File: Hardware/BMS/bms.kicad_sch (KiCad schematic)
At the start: 25 parts, among them J101 Conn_01x02, J102 Conn_02x05_Top_Bottom, J103 Conn_02x02_Counter_Clockwise, SW101 SW_MEC_5E, SW102 SW_SPDT, U102 STM32G473CCTx, U103 LTV-356T, U104 TCAN1042VDRQ1, Y101 48 MHZ

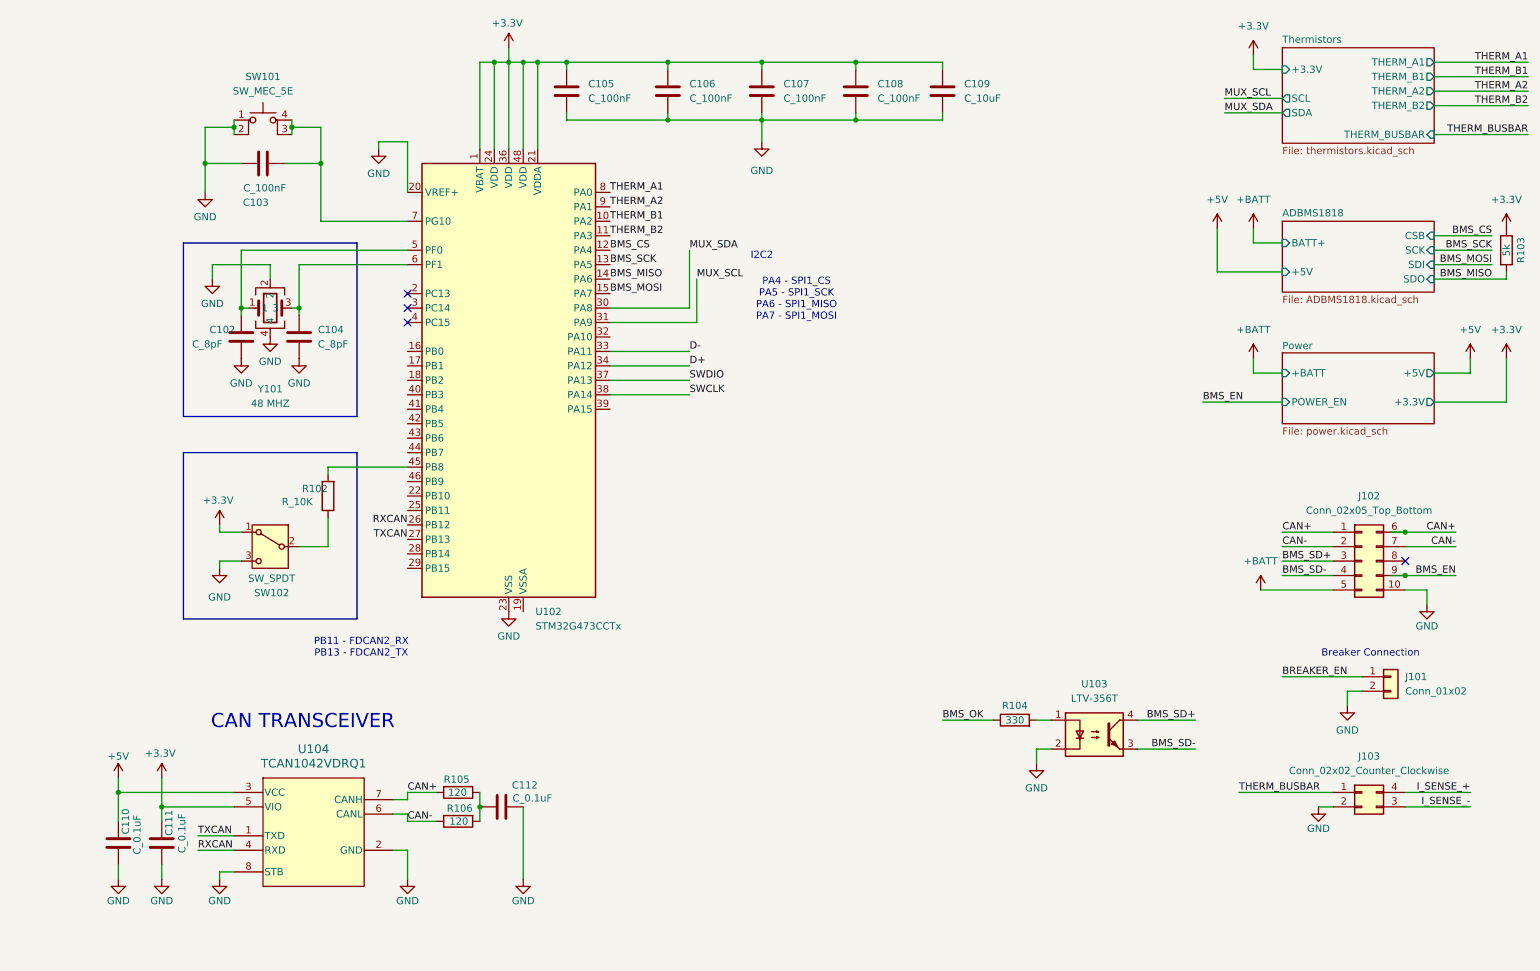
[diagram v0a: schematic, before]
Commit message: updated some stm stuff and added current sense amplifier for main pack
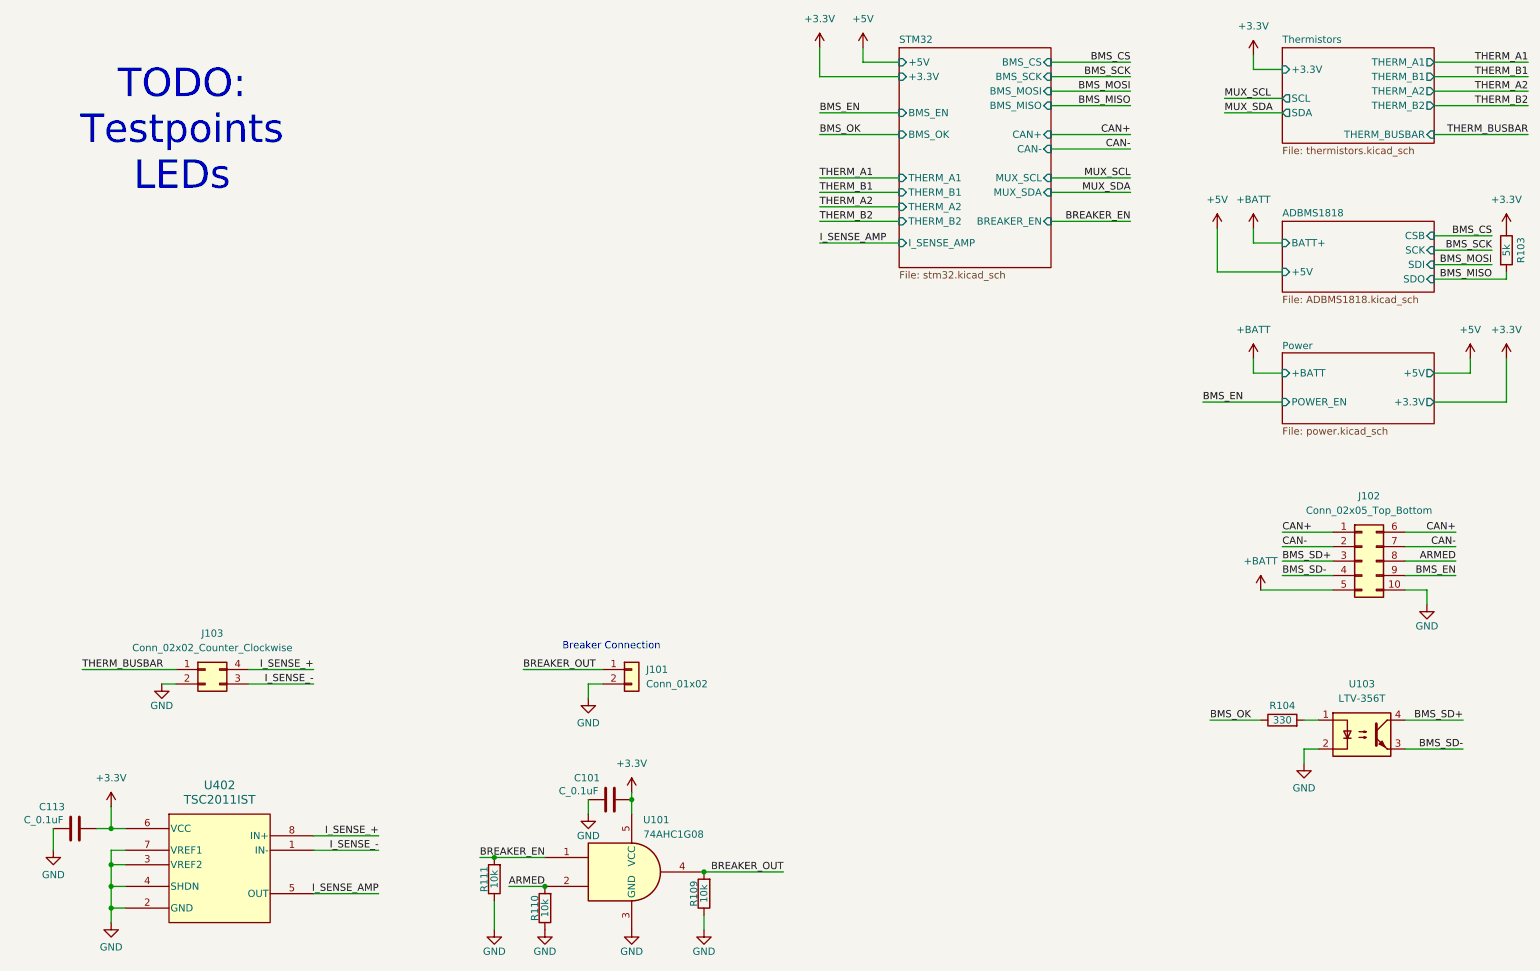
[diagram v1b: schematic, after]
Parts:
- removed C102, C104: C_8pF, OEM:C_0603_1608Metric, symbol formula:C_100nF
- removed C103, C105, C106, C107, C108: C_100nF, OEM:C_0603_1608Metric, symbol formula:C_100nF
- removed C109: C_10uF, footprints:C_0805_OEM, symbol formula:C_10uF
- removed C110, C111, C112: C_0.1uF, OEM:C_0603_1608Metric, symbol OEM:0u1F
- removed R102: R_10K, footprints:R_0805_OEM, symbol formula:R_10K
- removed R105, R106: 120, OEM:R_0603_1608Metric, symbol OEM:120R_DNP
- removed SW101: SW_MEC_5E, symbol Switch:SW_MEC_5E
- removed SW102: SW_SPDT, symbol Switch:SW_SPDT
- removed U102: STM32G473CCTx, Package_QFP:LQFP-48_7x7mm_P0.5mm, symbol MCU_ST_STM32G4:STM32G473CCTx
- removed U104: TCAN1042VDRQ1, BAD_LIB:D0008A_M, symbol OlinBAD:TCAN1042VDRQ1
- removed Y101: 48 MHZ, footprints:SMD_72002_TXC, symbol formula:Crystal_48MHz_8pF
- added C101, C113: C_0.1uF, OEM:C_0603_1608Metric, symbol OEM:0u1F
- added R109, R110, R111: 10k, Resistor_SMD:R_0603_1608Metric, symbol Device:R
- added U101: 74AHC1G08, OEM:SOT-23-5, symbol 74xGxx:74AHC1G08
- added U402: TSC2011IST, BAD_LIB:SO_011IST_STM-M, symbol OlinBAD:TSC2011IST
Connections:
- net +3.3V: now also C101.2, C113.2, U101.5 (VCC), U402.6 (VCC)
- net BREAKER_EN: now also R111.2, U101.1; no longer J101.1 (Pin_1)
- net GND: now also C101.1, C113.1, R109.1, R110.1, R111.1, U101.3 (GND), U402.2 (GND), U402.3 (VREF2), U402.4 (SHDN), U402.7 (VREF1)
- net I_SENSE_+: now also U402.8 (IN+)
- net I_SENSE_-: now also U402.1 (IN-)
- net ARMED: now reaches J102.8 (Pin_8)
- net ARMED: now also R110.2, U101.2
- new net BREAKER_OUT: J101.1 (Pin_1), R109.2, U101.4
- new net I_SENSE_AMP: U402.5 (OUT)
- no-connect marks 4 -> 0
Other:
- added sheet STM32 (stm32.kicad_sch)
- note added: "TODO: Testpoints LEDs"
- note removed: "CAN TRANSCEIVER"
- note removed: "I2C2"
- note removed: "PA4 - SPI1_CS PA5 - SPI1_SCK PA6 - SPI1_MISO PA7 - SPI1_MOSI"
- note removed: "PB11 - FDCAN2_RX PB13 - FDCAN2_TX"
- moved on the sheet: J101, J103, R104, U103
